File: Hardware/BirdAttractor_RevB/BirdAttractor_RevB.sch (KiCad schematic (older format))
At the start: 12 parts, among them P1 CONN_01X06, U1 PR_Relay_V23079, U2 DS1305, Y1 Crystal_Small

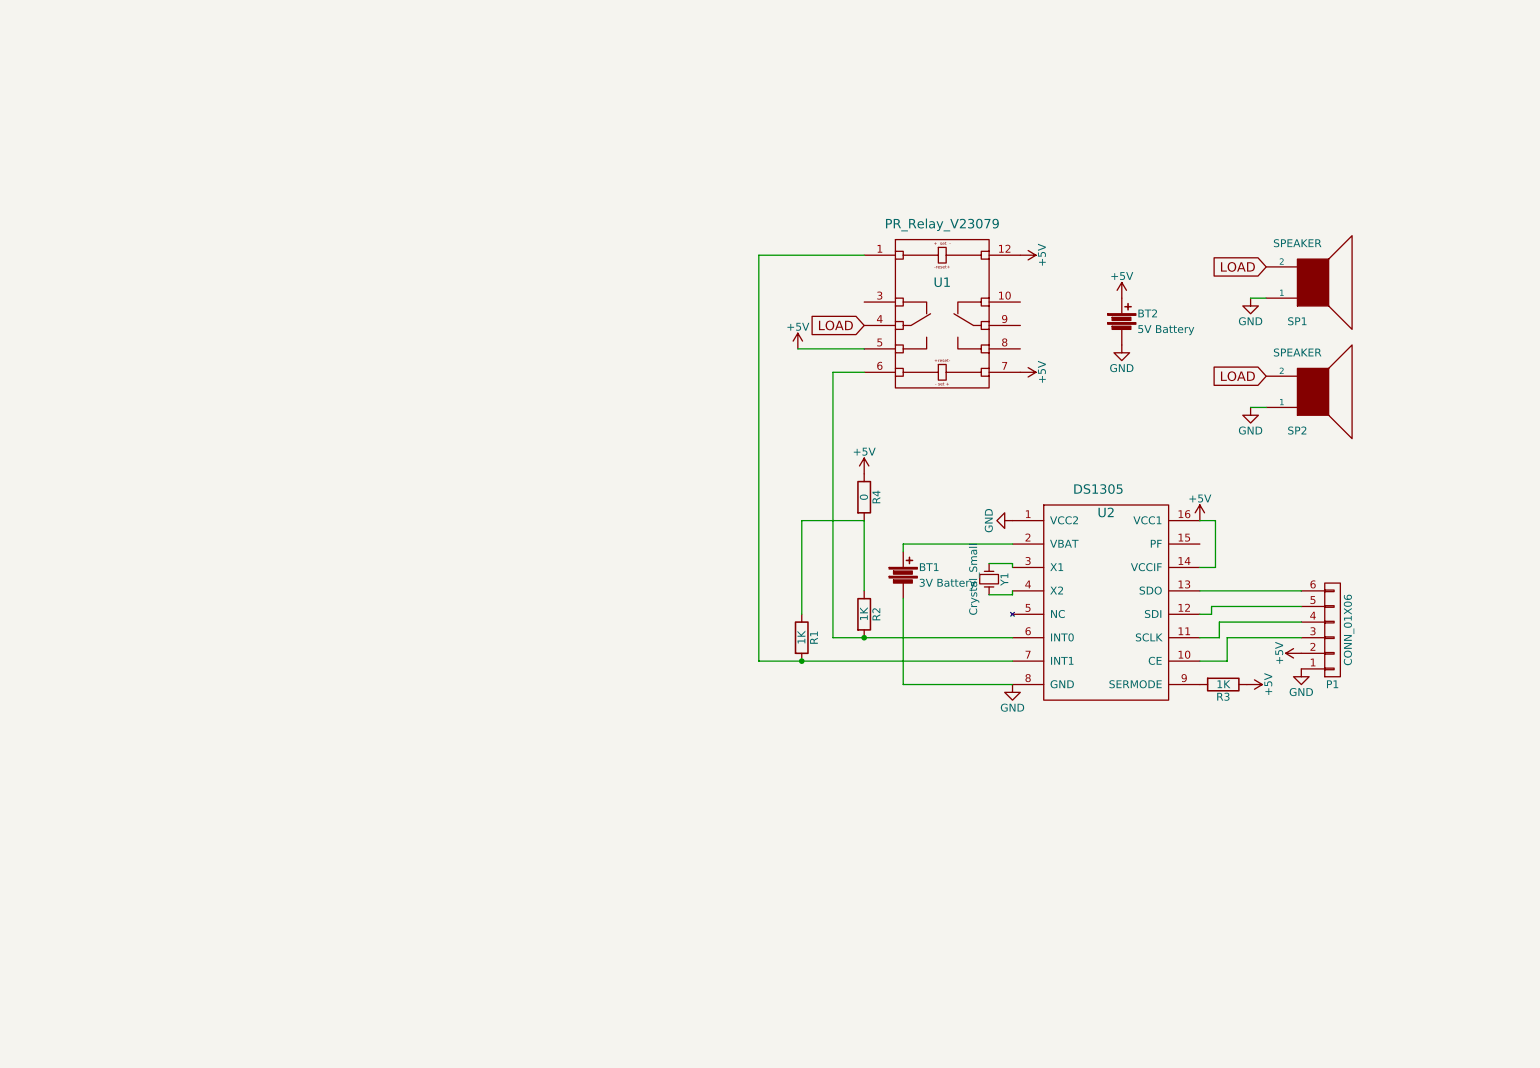
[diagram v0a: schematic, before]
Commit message: added notes on parts in readme, added new revision to the board with newly selected parts
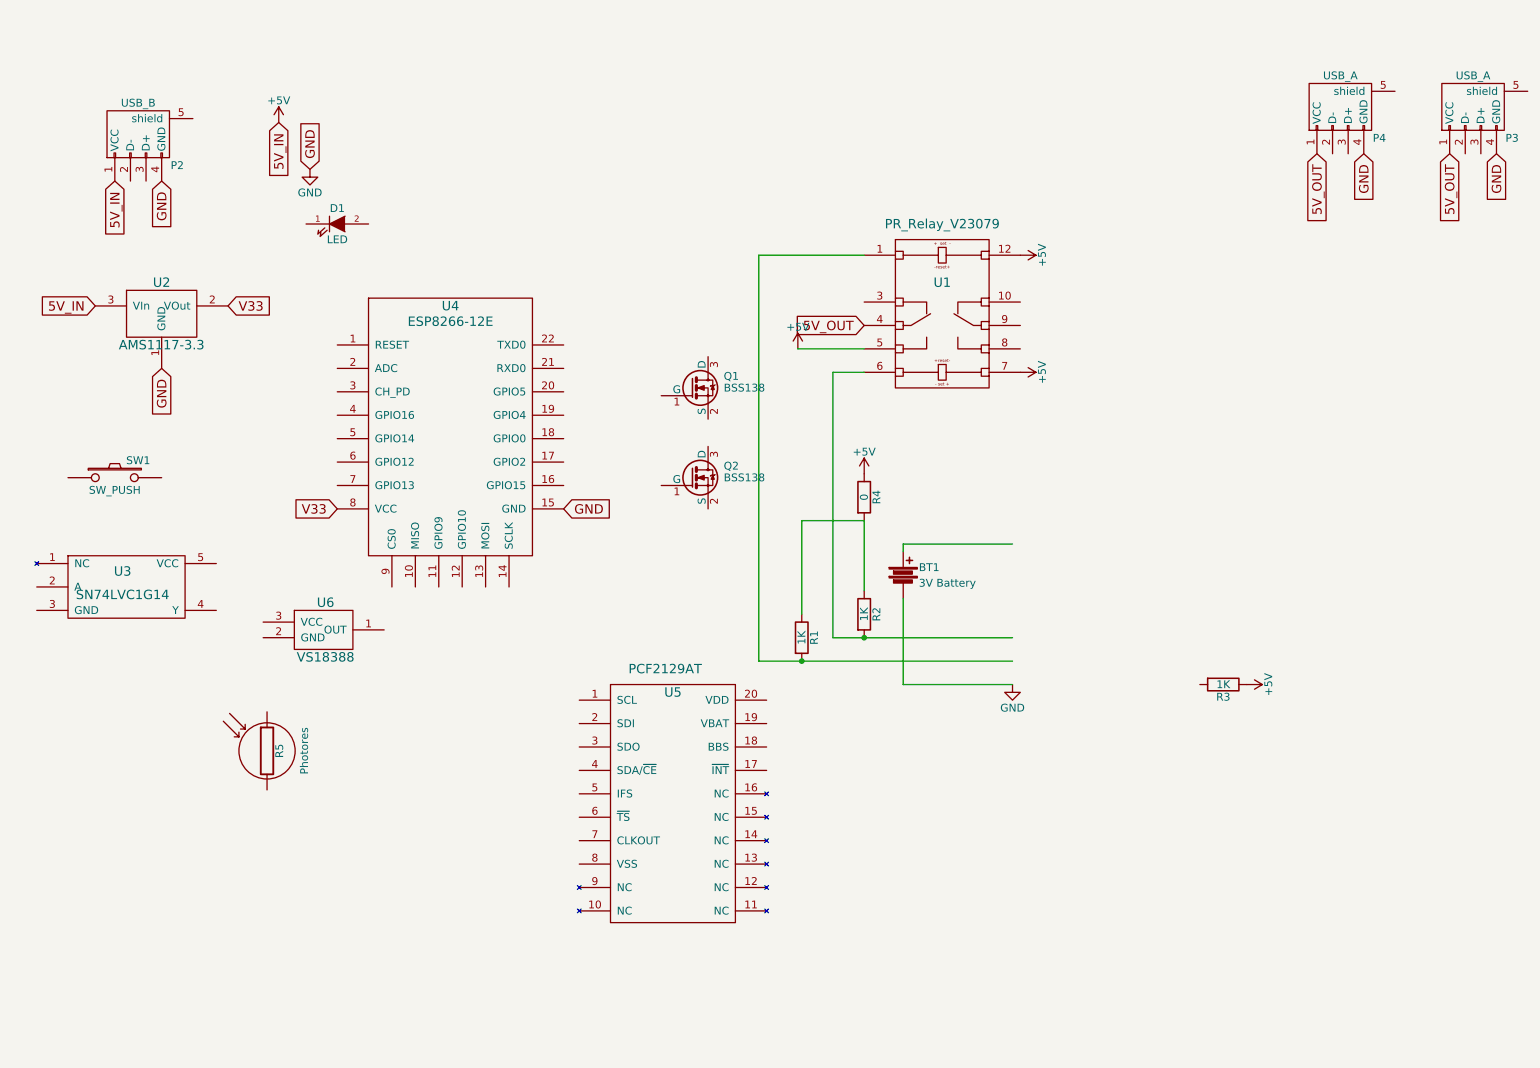
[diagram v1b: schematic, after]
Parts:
- removed BT2: 5V Battery, Terminal_Blocks:TerminalBlock_Pheonix_MPT-2.54mm_2pol, symbol Battery
- removed P1: CONN_01X06, Socket_Strips:Socket_Strip_Straight_1x06, symbol CONN_01X06
- removed SP1, SP2: SPEAKER, Terminal_Blocks:TerminalBlock_Pheonix_MPT-2.54mm_2pol, symbol SPEAKER
- removed U2: DS1305, Housings_DIP:DIP-16_W7.62mm, symbol DS1305
- removed Y1: Crystal_Small, Resistors_SMD:R_1218, symbol Crystal_Small
- added D1: LED, LEDs:LED-0805, symbol LED
- added P2: USB_B, Connect:USB_B, symbol USB_B
- added P3, P4: USB_A, Connect:USB_A, symbol USB_A
- added Q1, Q2: BSS138, TO_SOT_Packages_SMD:SOT-23, symbol BSS138
- added R5: Photores, LEDs:LED-3MM, symbol Photores
- added SW1: SW_PUSH, Buttons_Switches_SMD:SW_SPST_PTS645, symbol SW_PUSH
- added U2: AMS1117-3.3, TO_SOT_Packages_SMD:SOT89-3_Housing, symbol AMS1117-3.3
- added U3: SN74LVC1G14, MyKiCadParts:SOT-23-5-80, symbol SN74LVC1G14
- added U4: ESP8266-12E, MyKiCadParts:ESP8266-12E-80, symbol ESP8266-12E
- added U5: PCF2129AT, MyKiCadParts:SOIC-20_7.5x12.8mm_Pitch1.27mm-80, symbol PCF2129AT
- added U6: VS18388, Pin_Headers:Pin_Header_Straight_1x03, symbol VS18388
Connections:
- net labels added: 5V_IN, 5V_OUT, V33
- net labels removed: LOAD
- wire segments 33 -> 14

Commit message: added more components and more notes in the readme
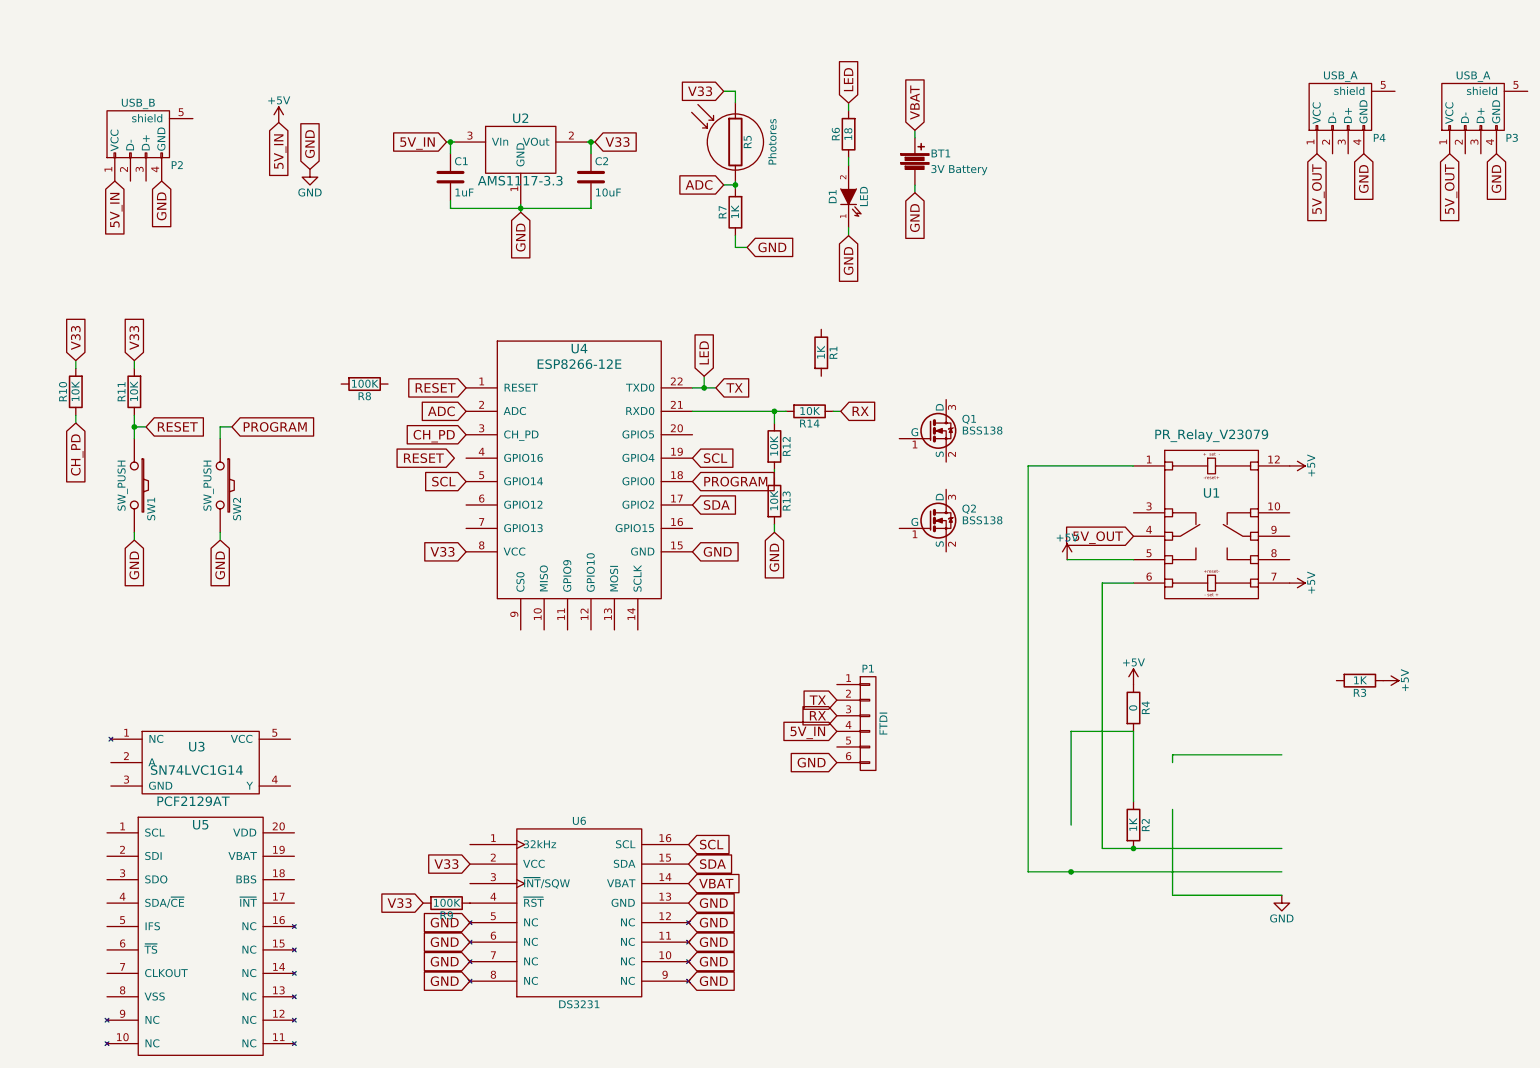
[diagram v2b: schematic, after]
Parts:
- removed U6: VS18388, Pin_Headers:Pin_Header_Straight_1x03, symbol VS18388
- added C1: 1uF, Capacitors_SMD:C_0805, symbol C
- added C2: 10uF, Capacitors_SMD:C_0805, symbol C
- added P1: FTDI, symbol CONN_01X06
- added R10, R11: 10K, Capacitors_SMD:C_1206, symbol R
- added R12, R13, R14: 10K, Resistors_SMD:R_1206, symbol R
- added R6: 18, Capacitors_SMD:C_1206, symbol R
- added R7: 1K, Capacitors_SMD:C_1206, symbol R
- added R8, R9: 100K, Capacitors_SMD:C_1206, symbol R
- added SW2: SW_PUSH, Buttons_Switches_SMD:SW_SPST_PTS645, symbol SW_PUSH
- added U6: DS3231, SMD_Packages:SO-16-W, symbol DS3231
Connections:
- net labels added: ADC, CH_PD, LED, PROGRAM, RESET, RX, SCL, SDA, TX, VBAT
- wire segments 14 -> 49
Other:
- moved on the sheet: BT1, D1, Q1, Q2, R1, R2, R3, R4, R5, SW1, U1, U2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

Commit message: added low pass debounce filter, added connections for different wake up functions, began layout design for in house pcb.
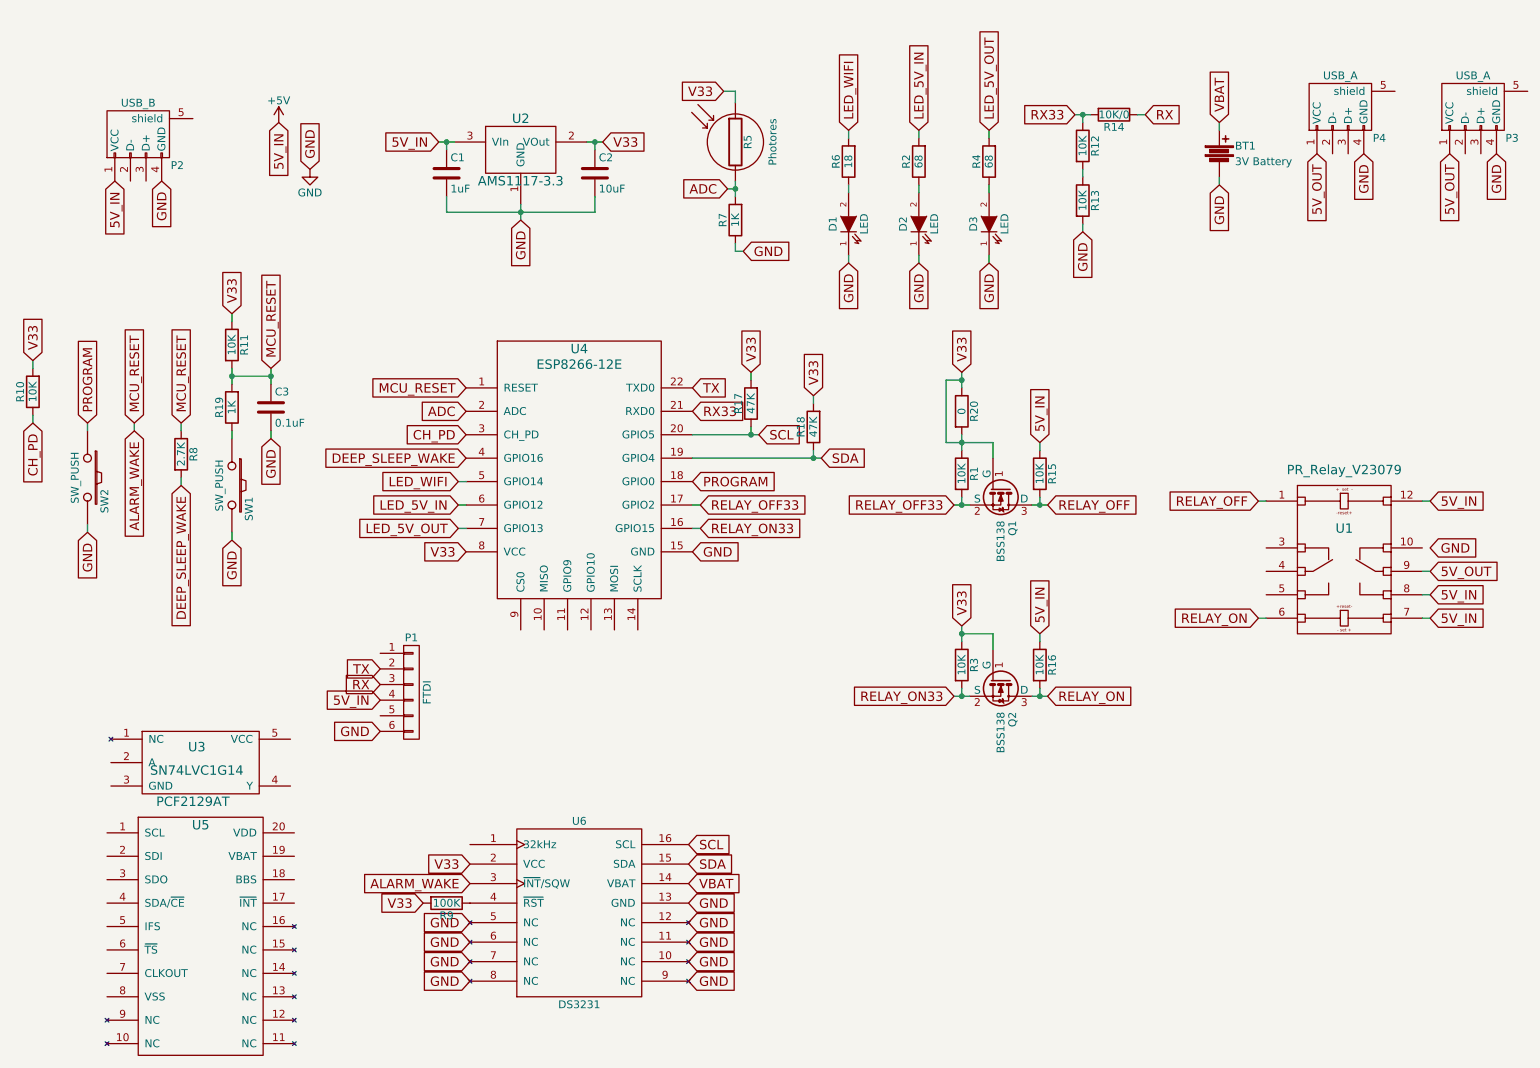
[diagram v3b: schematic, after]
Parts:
- added C3: 0.1uF, Capacitors_SMD:C_0805, symbol C
- added D2, D3: LED, LEDs:LED-0805, symbol LED
- added R15, R16: 10K, Resistors_SMD:R_1206, symbol R
- added R17, R18: 47K, Capacitors_SMD:C_1206, symbol R
- added R19: 1K, Capacitors_SMD:C_1206, symbol R
- added R20: 0, Resistors_SMD:R_1206, symbol R
- P1: footprint (none) -> Pin_Headers:Pin_Header_Angled_1x06
- R1, R3: value 1K -> 10K
- R14: value 10K -> 10K/0
- R2: value 1K -> 68; footprint Resistors_SMD:R_1206 -> Capacitors_SMD:C_1206
- R4: value 0 -> 68; footprint Resistors_SMD:R_1206 -> Capacitors_SMD:C_1206
- R8: value 100K -> 2.7K
- U2: footprint TO_SOT_Packages_SMD:SOT89-3_Housing -> TO_SOT_Packages_SMD:SOT-223
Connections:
- net labels added: ALARM_WAKE, DEEP_SLEEP_WAKE, LED_5V_IN, LED_5V_OUT, LED_WIFI, MCU_RESET, RELAY_OFF, RELAY_OFF33, RELAY_ON, RELAY_ON33, RX33
- net labels removed: LED, RESET
- wire segments 49 -> 80
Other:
- moved on the sheet: BT1, C1, C2, D1, P1, Q1, Q2, R1, R10, R11, R12, R13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
